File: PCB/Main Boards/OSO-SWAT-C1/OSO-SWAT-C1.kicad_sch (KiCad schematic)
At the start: 37 parts, among them J1 OSO_SWD, J2 FH19C-9S-0.5SH_10_, Q1 Q_Photo_NPN, U1 ATSAML22J18A-MUT, U2 MIC5365-3.3YC5-TR, X1 Crystal

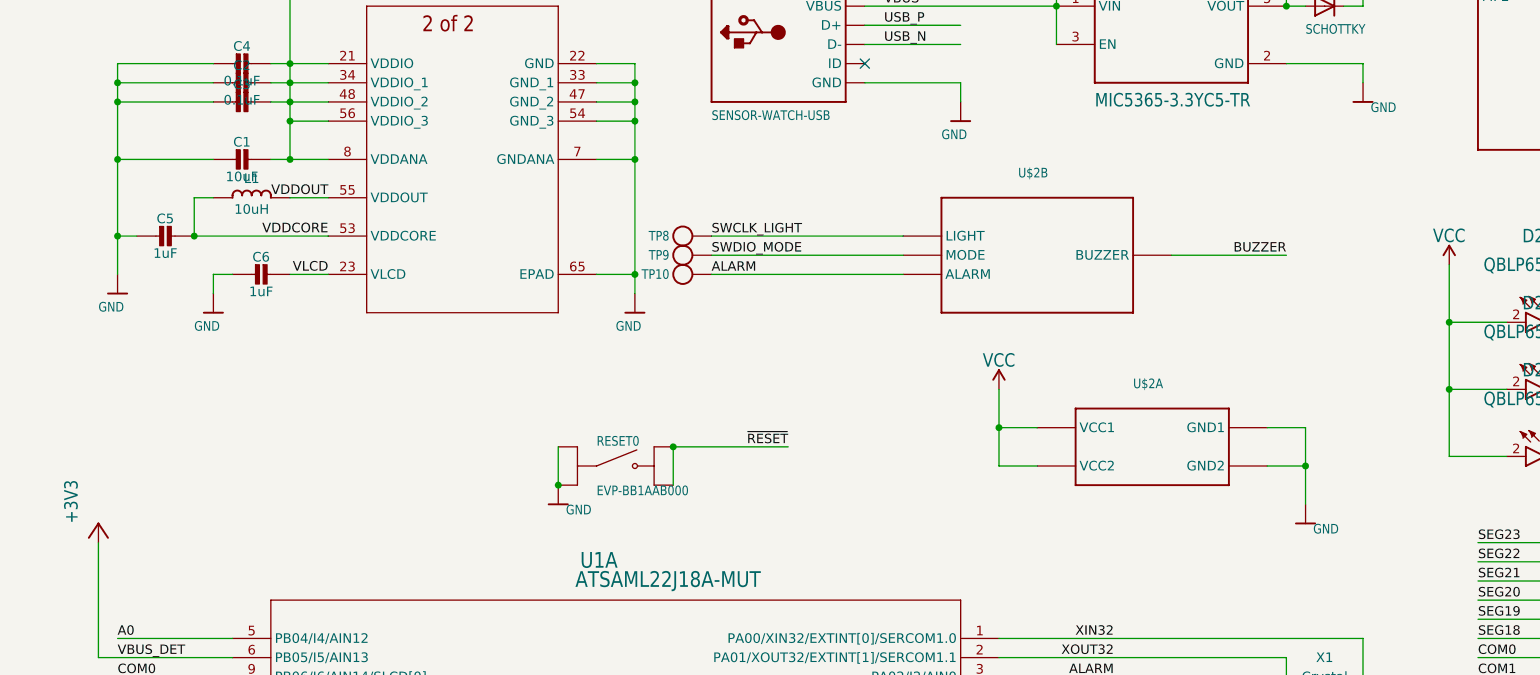
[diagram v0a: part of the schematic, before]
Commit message: WIP high voltage buzzer driver
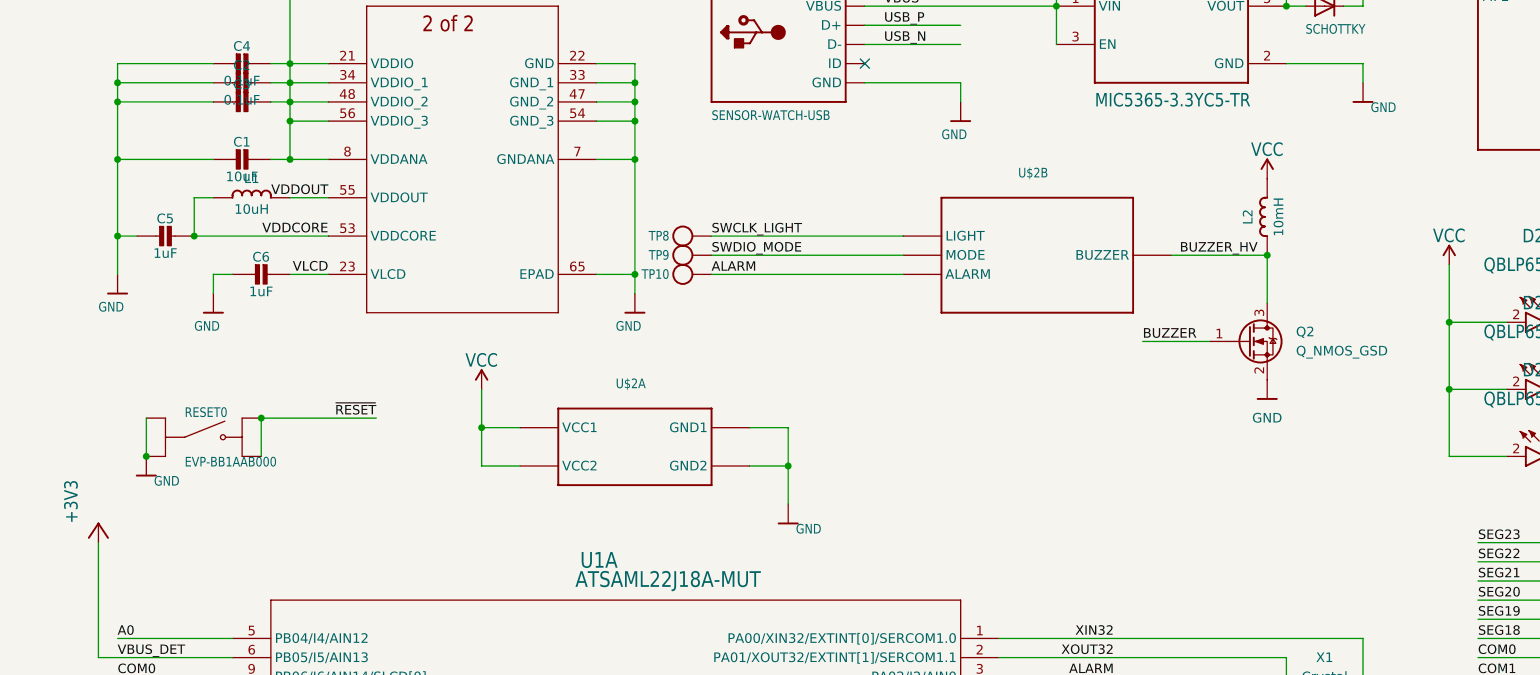
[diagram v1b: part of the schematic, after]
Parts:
- added L2: 10mH, Inductor_SMD:L_0603_1608Metric, symbol OSO-SWAT-A1-05-eagle-import:MICROBUILDER_INDUCTOR_0805MP
- added Q2: Q_NMOS_GSD, Package_TO_SOT_SMD:SOT-323_SC-70, symbol Device:Q_NMOS_GSD
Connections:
- net BUZZER: now also Q2.1 (G); no longer U$2.BUZZER
- net GND: now also Q2.2 (S)
- net VCC: now also L2.2
- new net BUZZER_HV: L2.1, Q2.3 (D), U$2.BUZZER
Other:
- moved on the sheet: RESET0, U$2A
